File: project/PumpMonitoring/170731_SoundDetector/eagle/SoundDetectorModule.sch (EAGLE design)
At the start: 32 parts, among them CN1 JST-PH-K*, IC1 LMV324

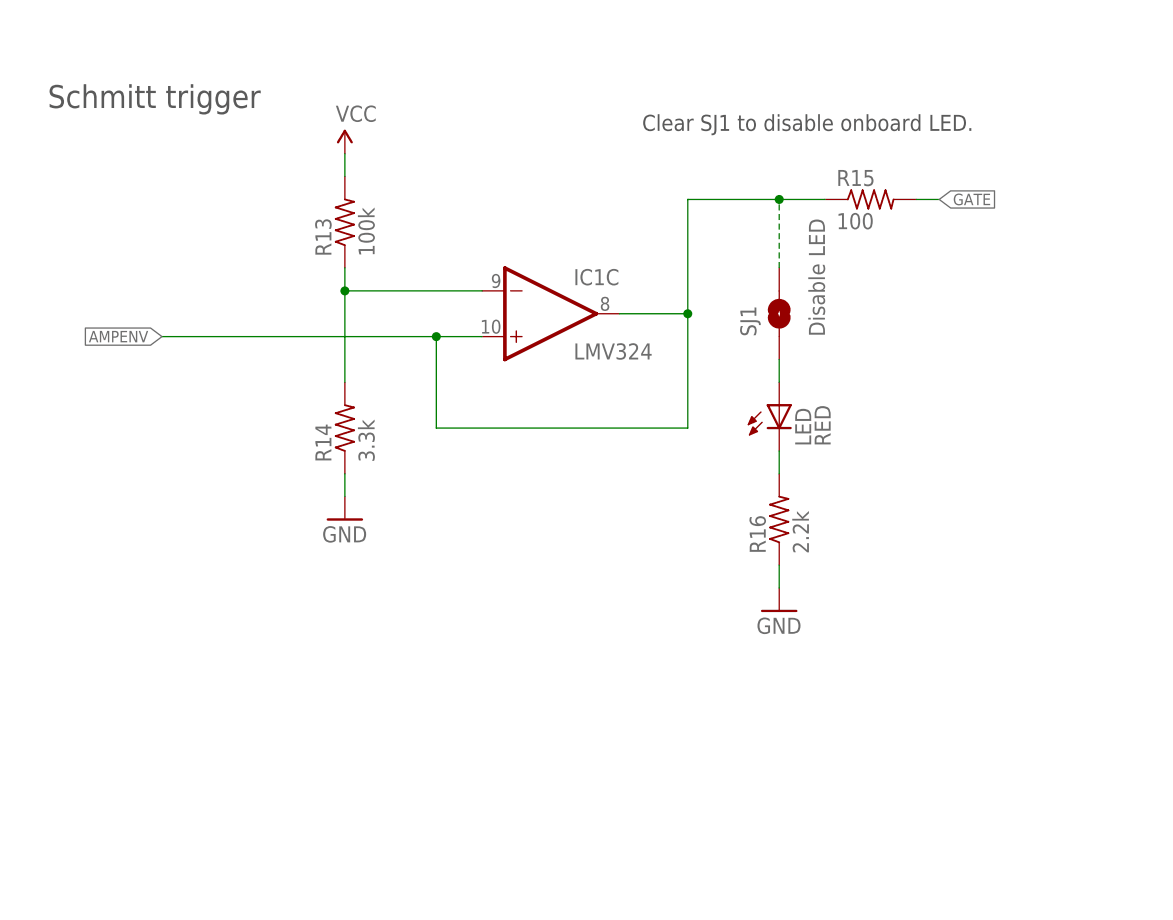
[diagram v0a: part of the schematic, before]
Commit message: update sound detector module
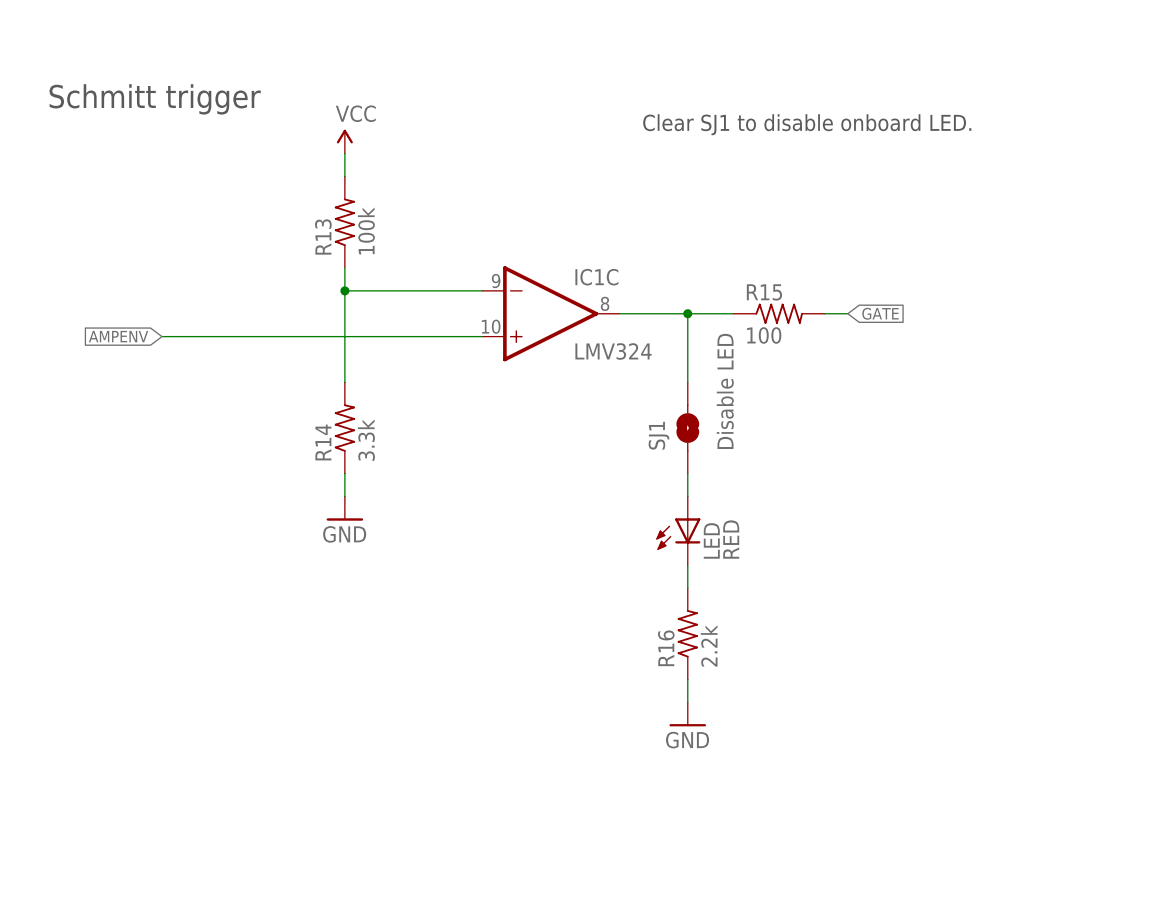
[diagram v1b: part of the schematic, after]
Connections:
- new net N$16: IC1C.OUT, R15.1, SJ1.2
- net AMPENV: no longer IC1C.OUT, R15.1, SJ1.2
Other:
- moved on the sheet: LED, R15, R16, SJ1
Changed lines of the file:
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@@
 <instance part="SUPPLY4" gate="1" x="231.14" y="106.68"/>
 <instance part="GND8" gate="1" x="231.14" y="66.04"/>
-<instance part="R15" gate="G$1" x="289.56" y="101.6"/>
-<instance part="R16" gate="G$1" x="279.4" y="66.04" rot="R90"/>
-<instance part="LED" gate="G$1" x="279.4" y="76.2"/>
-<instance part="GND1" gate="1" x="279.4" y="55.88"/>
+<instance part="R15" gate="G$1" x="279.4" y="88.9"/>
+<instance part="R16" gate="G$1" x="269.24" y="53.34" rot="R90"/>
+<instance part="LED" gate="G$1" x="269.24" y="63.5"/>
+<instance part="GND1" gate="1" x="269.24" y="43.18"/>
 <instance part="C4" gate="G$1" x="172.72" y="149.86" rot="R90"/>
 <instance part="C6" gate="G$1" x="152.4" y="91.44"/>
 <instance part="GND9" gate="1" x="152.4" y="81.28"/>
 <instance part="SUPPLY5" gate="1" x="152.4" y="96.52"/>
-<instance part="SJ1" gate="1" x="279.4" y="88.9" rot="R90"/>
+<instance part="SJ1" gate="1" x="269.24" y="76.2" rot="R90"/>
 <instance part="R8" gate="G$1" x="208.28" y="172.72"/>
 <instance part="R12" gate="G$1" x="294.64" y="139.7"/>
@@
 <pinref part="R16" gate="G$1" pin="1"/>
 <pinref part="GND1" gate="1" pin="GND"/>
-<wire x1="279.4" y1="60.96" x2="279.4" y2="58.42" width="0.1524" layer="91"/>
+<wire x1="269.24" y1="48.26" x2="269.24" y2="45.72" width="0.1524" layer="91"/>
 </segment>
 <segment>
@@
 </segment>
 <segment>
+<pinref part="IC1" gate="C" pin="+IN"/>
+<wire x1="210.82" y1="86.36" x2="246.38" y2="86.36" width="0.1524" layer="91"/>
 <label x="210.82" y="86.36" size="1.27" layer="95" rot="R180" xref="yes"/>
-<wire x1="241.3" y1="86.36" x2="241.3" y2="76.2" width="0.1524" layer="91"/>
-<wire x1="246.38" y1="86.36" x2="241.3" y2="86.36" width="0.1524" layer="91"/>
-<junction x="241.3" y="86.36"/>
-<wire x1="210.82" y1="86.36" x2="241.3" y2="86.36" width="0.1524" layer="91"/>
-<pinref part="R15" gate="G$1" pin="1"/>
-<wire x1="269.24" y1="76.2" x2="269.24" y2="88.9" width="0.1524" layer="91"/>
-<wire x1="269.24" y1="88.9" x2="269.24" y2="101.6" width="0.1524" layer="91"/>
-<wire x1="269.24" y1="101.6" x2="279.4" y2="101.6" width="0.1524" layer="91"/>
-<pinref part="SJ1" gate="1" pin="2"/>
-<wire x1="279.4" y1="101.6" x2="284.48" y2="101.6" width="0.1524" layer="91"/>
-<wire x1="279.4" y1="93.98" x2="279.4" y2="101.6" width="0.1524" layer="91" style="longdash"/>
-<junction x="279.4" y="101.6"/>
-<wire x1="241.3" y1="76.2" x2="269.24" y2="76.2" width="0.1524" layer="91"/>
-<pinref part="IC1" gate="C" pin="+IN"/>
-<pinref part="IC1" gate="C" pin="OUT"/>
-<wire x1="261.62" y1="88.9" x2="269.24" y2="88.9" width="0.1524" layer="91"/>
-<junction x="269.24" y="88.9"/>
 </segment>
 </net>
@@
 <segment>
 <pinref part="R15" gate="G$1" pin="2"/>
-<wire x1="294.64" y1="101.6" x2="297.18" y2="101.6" width="0.1524" layer="91"/>
-<label x="297.18" y="101.6" size="1.27" layer="95" xref="yes"/>
+<wire x1="284.48" y1="88.9" x2="287.02" y2="88.9" width="0.1524" layer="91"/>
+<label x="287.02" y="88.9" size="1.27" layer="95" xref="yes"/>
 </segment>
 <segment>
@@
 <pinref part="R16" gate="G$1" pin="2"/>
 <pinref part="LED" gate="G$1" pin="C"/>
-<wire x1="279.4" y1="71.12" x2="279.4" y2="73.66" width="0.1524" layer="91"/>
+<wire x1="269.24" y1="58.42" x2="269.24" y2="60.96" width="0.1524" layer="91"/>
 </segment>
 </net>
@@
 <pinref part="LED" gate="G$1" pin="A"/>
 <pinref part="SJ1" gate="1" pin="1"/>
-<wire x1="279.4" y1="81.28" x2="279.4" y2="83.82" width="0.1524" layer="91"/>
+<wire x1="269.24" y1="68.58" x2="269.24" y2="71.12" width="0.1524" layer="91"/>
 </segment>
 </net>
@@
 </segment>
 </net>
+<net name="N$16" class="0">
+<segment>
+<pinref part="R15" gate="G$1" pin="1"/>
+<wire x1="269.24" y1="88.9" x2="274.32" y2="88.9" width="0.1524" layer="91"/>
+<pinref part="SJ1" gate="1" pin="2"/>
+<wire x1="269.24" y1="88.9" x2="269.24" y2="81.28" width="0.1524" layer="91"/>
+<pinref part="IC1" gate="C" pin="OUT"/>
+<wire x1="261.62" y1="88.9" x2="269.24" y2="88.9" width="0.1524" layer="91"/>
+<junction x="269.24" y="88.9"/>
+</segment>
+</net>
